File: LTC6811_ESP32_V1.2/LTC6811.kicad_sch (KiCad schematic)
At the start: 61 parts, among them J10 Hole /NC, J11 Hole /NC, J12 Hole /NC, J13 B7B-XH-A, J14 B7B-XH-A, J15 PB MB, Q2 NSV1C201MZ4, U12 LTC6811HG-1

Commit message: Add files via upload
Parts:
- removed J10, J11, J12: Hole /NC, MountingHole:MountingHole_3.2mm_M3_ISO7380_Pad, symbol Connector_Generic:Conn_01x01
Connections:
- no-connect marks 7 -> 4
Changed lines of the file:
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@@
   )
   (no_connect (at 331.47 65.405))
-  (no_connect (at 33.02 40.005))
   (no_connect (at 199.39 131.445))
-  (no_connect (at 33.02 52.705))
   (no_connect (at 199.39 128.905))
-  (no_connect (at 33.02 46.355))
   (no_connect (at 331.47 50.165))
   (wire (pts (xy 143.51 149.225) (xy 173.99 149.225))
@@
     (stroke (width 0) (type default))
   )
-  (polyline (pts (xy 316.23 31.75) (xy 316.23 100.33))
-    (stroke (width 1) (type dash) (color 33 12 255 1))
-  )
   (wire (pts (xy 111.76 183.515) (xy 100.33 183.515))
     (stroke (width 0) (type default))
@@
   (hierarchical_label "MA" (shape input) (at 348.615 60.325 0) (fields_autoplaced)
     (effects (font (size 1.27 1.27)) (justify left))
-  )
-  (symbol (lib_id "Connector_Generic:Conn_01x01") (at 27.94 46.355 180) (unit 1)
-    (in_bom yes) (on_board yes) (dnp no)
-    (property "Reference" "J11" (at 30.0228 42.9768 0)
-      (effects (font (size 1.27 1.27)))
-    )
-    (property "Value" "Hole /NC" (at 30.0228 42.9514 0)
-      (effects (font (size 1.27 1.27)) hide)
-    )
-    (property "Footprint" "MountingHole:MountingHole_3.2mm_M3_ISO7380_Pad" (at 27.94 46.355 0)
-      (effects (font (size 1.27 1.27)) hide)
-    )
-    (property "Datasheet" "~" (at 27.94 46.355 0)
-      (effects (font (size 1.27 1.27)) hide)
-    )
-    (property "MPN" "N/A" (at 27.94 46.355 0)
-      (effects (font (size 1.27 1.27)) hide)
-    )
-    (pin "1")
-    (instances
-      (project "LTC6811_ESP32_V1.2"
-        (path "/6a86ff6f-b159-4c4c-8a40-e732cc82e010/0999518d-09c3-4a69-bd78-ff81b3ce8dd2"
-          (reference "J11") (unit 1)
-        )
-      )
-      (project "LTC6811"
-        (path "/c4061cfa-a05d-44c7-ba89-bb211c8b143a"
-          (reference "J6") (unit 1)
-        )
-      )
-    )
   )
   (symbol (lib_id "Diode:BZT52Bxx") (at 78.74 81.915 270) (unit 1)
@@
         (path "/c4061cfa-a05d-44c7-ba89-bb211c8b143a"
           (reference "R2") (unit 1)
-        )
-      )
-    )
-  )
-  (symbol (lib_id "Connector_Generic:Conn_01x01") (at 27.94 40.005 180) (unit 1)
-    (in_bom yes) (on_board yes) (dnp no)
-    (property "Reference" "J10" (at 30.0228 36.6268 0)
-      (effects (font (size 1.27 1.27)))
-    )
-    (property "Value" "Hole /NC" (at 30.0228 36.6014 0)
-      (effects (font (size 1.27 1.27)) hide)
-    )
-    (property "Footprint" "MountingHole:MountingHole_3.2mm_M3_ISO7380_Pad" (at 27.94 40.005 0)
-      (effects (font (size 1.27 1.27)) hide)
-    )
-    (property "Datasheet" "~" (at 27.94 40.005 0)
-      (effects (font (size 1.27 1.27)) hide)
-    )
-    (property "MPN" "N/A" (at 27.94 40.005 0)
-      (effects (font (size 1.27 1.27)) hide)
-    )
-    (pin "1")
-    (instances
-      (project "LTC6811_ESP32_V1.2"
-        (path "/6a86ff6f-b159-4c4c-8a40-e732cc82e010/0999518d-09c3-4a69-bd78-ff81b3ce8dd2"
-          (reference "J10") (unit 1)
-        )
-      )
-      (project "LTC6811"
-        (path "/c4061cfa-a05d-44c7-ba89-bb211c8b143a"
-          (reference "J5") (unit 1)
         )
       )
@@
         )
       )
-    )
-  )
-  (symbol (lib_id "Connector_Generic:Conn_01x01") (at 27.94 52.705 180) (unit 1)
-    (in_bom yes) (on_board yes) (dnp no)
-    (property "Reference" "J12" (at 30.0228 49.3268 0)
-      (effects (font (size 1.27 1.27)))
-    )
-    (property "Value" "Hole /NC" (at 30.0228 49.3014 0)
-      (effects (font (size 1.27 1.27)) hide)
-    )
-    (property "Footprint" "MountingHole:MountingHole_3.2mm_M3_ISO7380_Pad" (at 27.94 52.705 0)
-      (effects (font (size 1.27 1.27)) hide)
-    )
-    (property "Datasheet" "~" (at 27.94 52.705 0)
-      (effects (font (size 1.27 1.27)) hide)
-    )
-    (property "MPN" "N/A" (at 27.94 52.705 0)
-      (effects (font (size 1.27 1.27)) hide)
-    )
-    (pin "1")
-    (instances
-      (project "LTC6811_ESP32_V1.2"
-        (path "/6a86ff6f-b159-4c4c-8a40-e732cc82e010/0999518d-09c3-4a69-bd78-ff81b3ce8dd2"
-          (reference "J12") (unit 1)
-        )
-      )
-      (project "LTC6811"
-        (path "/c4061cfa-a05d-44c7-ba89-bb211c8b143a"
-          (reference "J8") (unit 1)
-        )
-      )

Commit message: finished
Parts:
- added TP3 (x2): TestPoint, TestPoint:TestPoint_Pad_D1.0mm, symbol Connector:TestPoint
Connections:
- net Vref2: now also TP3.1
- net Vreg: now also TP3.1
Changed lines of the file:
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@@
     (stroke (width 0) (type default))
   )
+  (wire (pts (xy 296.545 151.765) (xy 304.165 151.765))
+    (stroke (width 0) (type default))
+  )
   (wire (pts (xy 219.075 121.285) (xy 219.075 118.745))
     (stroke (width 0) (type default))
@@
     (stroke (width 0) (type default))
   )
+  (wire (pts (xy 296.545 156.845) (xy 304.165 156.845))
+    (stroke (width 0) (type default))
+  )
   (wire (pts (xy 78.74 55.245) (xy 92.71 55.245))
     (stroke (width 0) (type default))
@@
     (effects (font (size 1.27 1.27) (color 255 0 4 1)) (justify left bottom))
   )
+  (label "Vref2" (at 297.815 156.845 0) (fields_autoplaced)
+    (effects (font (size 1.27 1.27)) (justify left bottom))
+  )
   (label "T5" (at 339.725 193.675 180) (fields_autoplaced)
     (effects (font (size 1.27 1.27)) (justify right bottom))
@@
     (effects (font (size 1.27 1.27)) (justify left bottom))
   )
+  (label "Vreg" (at 297.815 151.765 0) (fields_autoplaced)
+    (effects (font (size 1.27 1.27)) (justify left bottom))
+  )
   (label "T4" (at 205.74 159.385 180) (fields_autoplaced)
     (effects (font (size 1.27 1.27)) (justify right bottom))
@@
     )
   )
+  (symbol (lib_id "Connector:TestPoint") (at 304.165 151.765 270) (unit 1)
+    (in_bom yes) (on_board yes) (dnp no)
+    (property "Reference" "TP3" (at 308.737 154.305 0)
+      (effects (font (size 1.27 1.27)) (justify left) hide)
+    )
+    (property "Value" "TestPoint" (at 309.245 151.765 90)
+      (effects (font (size 1.27 1.27)) (justify left))
+    )
+    (property "Footprint" "TestPoint:TestPoint_Pad_D1.0mm" (at 304.165 156.845 0)
+      (effects (font (size 1.27 1.27)) hide)
+    )
+    (property "Datasheet" "~" (at 304.165 156.845 0)
+      (effects (font (size 1.27 1.27)) hide)
+    )
+    (pin "1")
+    (instances
+      (project "LTC6811_ESP32_V1.2"
+        (path "/6a86ff6f-b159-4c4c-8a40-e732cc82e010/00000000-0000-0000-0000-00005ac18063"
+          (reference "TP3") (unit 1)
+        )
+        (path "/6a86ff6f-b159-4c4c-8a40-e732cc82e010/0999518d-09c3-4a69-bd78-ff81b3ce8dd2"
+          (reference "TP3") (unit 1)
+        )
+      )
+    )
+  )
   (symbol (lib_id "Device:R") (at 208.28 126.365 90) (unit 1)
     (in_bom yes) (on_board yes) (dnp no)
@@
     )
   )
+  (symbol (lib_id "Connector:TestPoint") (at 304.165 156.845 270) (unit 1)
+    (in_bom yes) (on_board yes) (dnp no)
+    (property "Reference" "TP3" (at 308.737 159.385 0)
+      (effects (font (size 1.27 1.27)) (justify left) hide)
+    )
+    (property "Value" "TestPoint" (at 309.245 156.845 90)
+      (effects (font (size 1.27 1.27)) (justify left))
+    )
+    (property "Footprint" "TestPoint:TestPoint_Pad_D1.0mm" (at 304.165 161.925 0)
+      (effects (font (size 1.27 1.27)) hide)
+    )
+    (property "Datasheet" "~" (at 304.165 161.925 0)
+      (effects (font (size 1.27 1.27)) hide)
+    )
+    (pin "1")
+    (instances
+      (project "LTC6811_ESP32_V1.2"
+        (path "/6a86ff6f-b159-4c4c-8a40-e732cc82e010/00000000-0000-0000-0000-00005ac18063"
+          (reference "TP3") (unit 1)
+        )
+        (path "/6a86ff6f-b159-4c4c-8a40-e732cc82e010/0999518d-09c3-4a69-bd78-ff81b3ce8dd2"
+          (reference "TP4") (unit 1)
+        )
+      )
+    )
+  )
   (symbol (lib_id "Device:Fuse") (at 68.58 159.385 90) (mirror x) (unit 1)
     (in_bom yes) (on_board yes) (dnp no)
@@
       (effects (font (size 1.27 1.27)))
     )
-    (property "Value" "LED Red" (at 360.045 95.885 0)
+    (property "Value" "LED Red" (at 363.22 99.695 90)
       (effects (font (size 1.27 1.27)))
     )

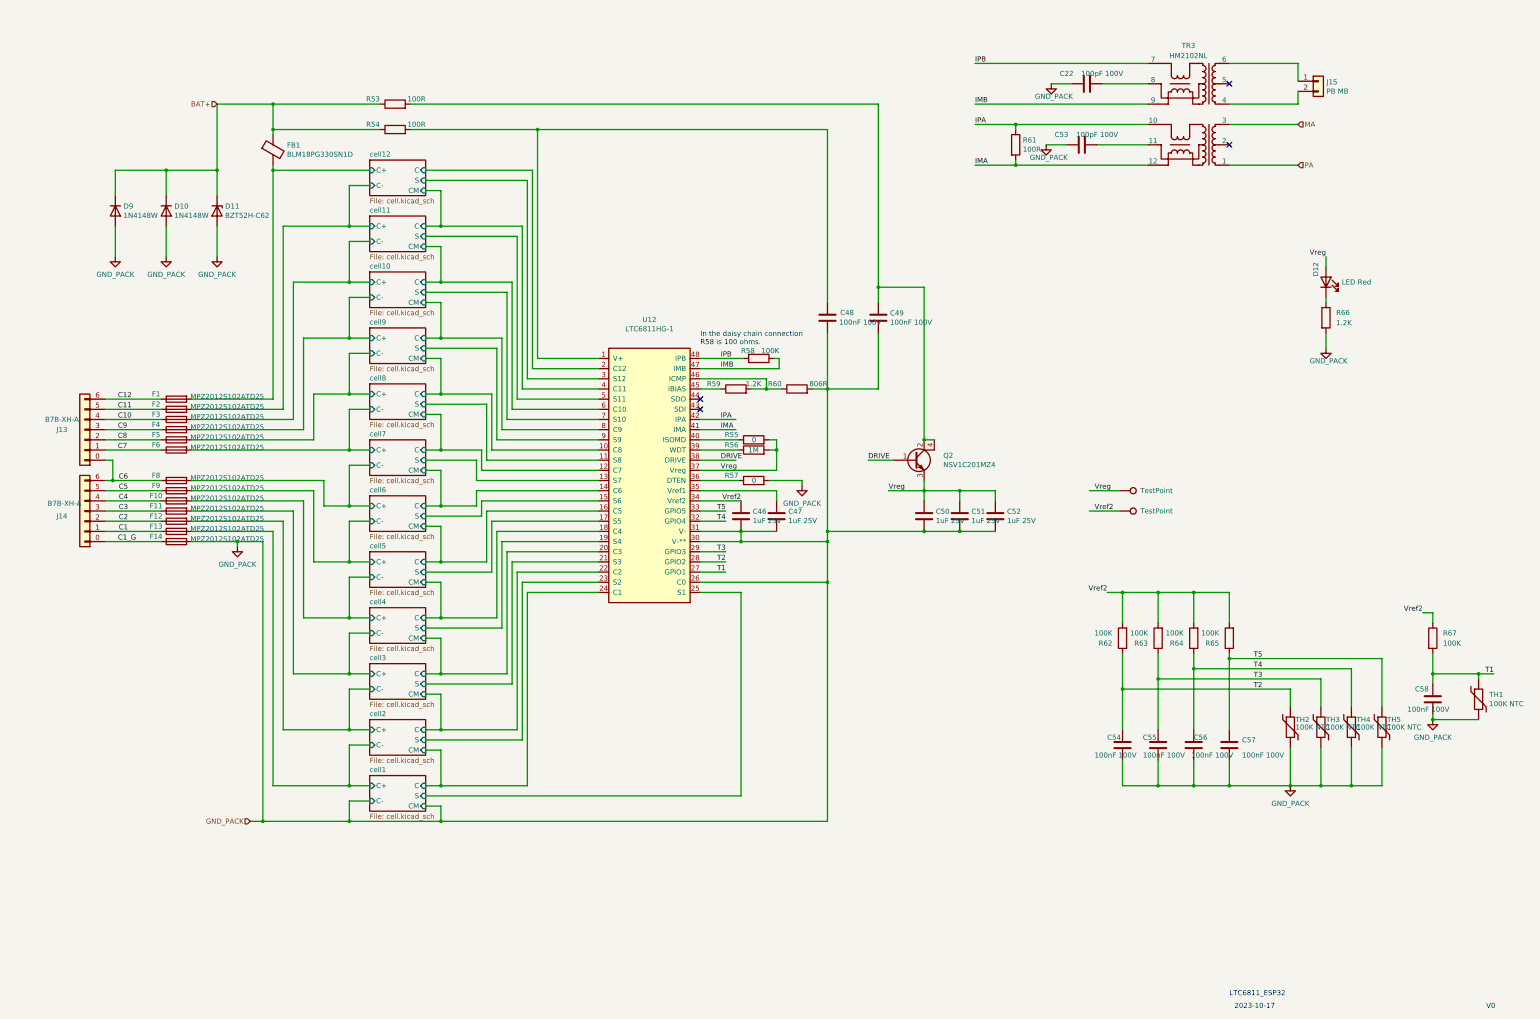
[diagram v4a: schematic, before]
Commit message: add BOM
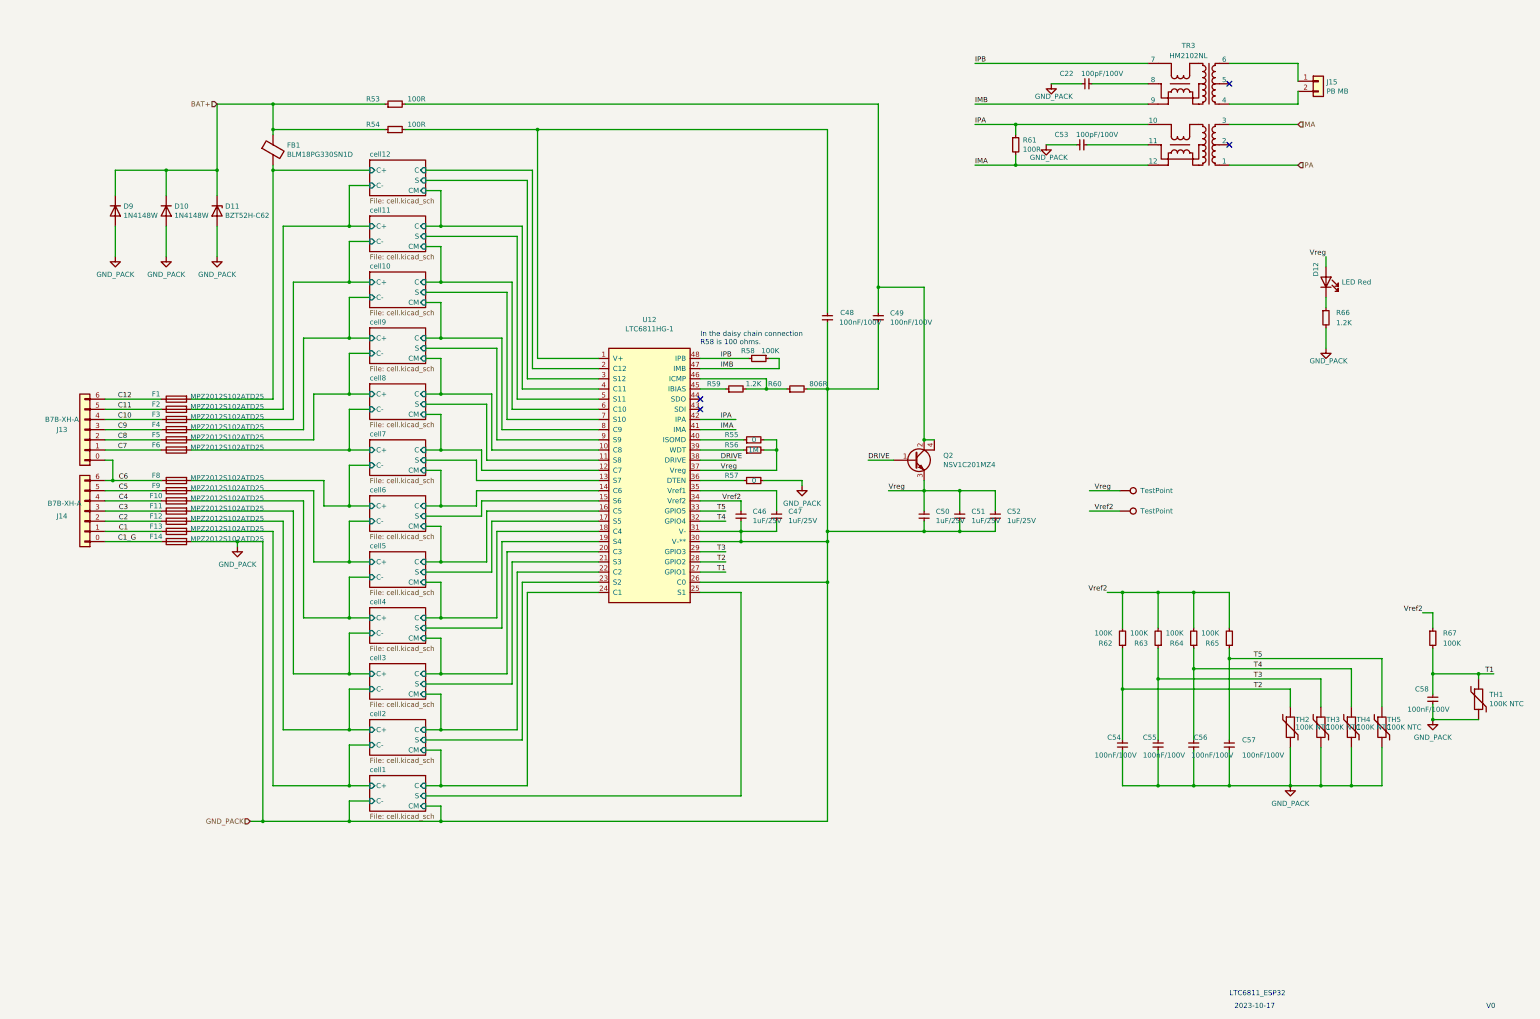
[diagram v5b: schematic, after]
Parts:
- C22, C53: value 100pF 100V -> 100pF/100V; symbol LTC6811-rescue:C-Device -> Device:C
- C46, C47, C50, C51, C52: value 1uF 25V -> 1uF/25V; symbol LTC6811-rescue:C-Device -> Device:C
- C48, C49, C54, C55, C56, C57, C58: value 100nF 100V -> 100nF/100V; symbol LTC6811-rescue:C-Device -> Device:C
- J15: Link https://www.digikey.jp/en/products/detail/molex/0705430001/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 -> https://www.digikey.jp/en/products/detail/jst-sales-america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; MPN 70543-0001 -> B2P-VH
- R53, R54, R55, R56, R57, R58, R59, R60, R61, R62, R63, R64, R65, R66, R67: symbol Device:R -> Device:R_Small
